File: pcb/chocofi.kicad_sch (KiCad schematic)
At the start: 154 parts, among them SW10 SW_PUSH, SW11 SW_PUSH, SW12 SW_PUSH, SW14 SW_PUSH, SW15 SW_PUSH, SW16 SW_PUSH, SW17 SW_PUSH, SW18 SW_PUSH, SW19 SW_PUSH, SW2 SW_PUSH, SW20 SW_PUSH, SW21 SW_PUSH, SW23 SW_PUSH, SW24 SW_PUSH, SW25 SW_PUSH, SW26 SW_PUSH, SW27 SW_PUSH, SW29 SW_PUSH, SW3 SW_PUSH, SW30 SW_PUSH, SW31 SW_PUSH, SW32 SW_PUSH, SW33 SW_PUSH, SW35 SW_PUSH, SW36 SW_PUSH, SW37 SW_PUSH, SW38 SW_PUSH, SW39 SW_PUSH, SW4 SW_PUSH, SW40 SW_PUSH, SW41 SW_PUSH, SW42 SW_PUSH, SW5 SW_PUSH, SW6 SW_PUSH, SW8 SW_PUSH, SW9 SW_PUSH, U1 nice_nano, U2 nice_nano

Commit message: feat: update
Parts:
- C1, C10, C11, C12, C13, C14, C15, C16, C17, C18, C19, C2, C20, C21, C22, C23, C24, C25, C26, C27, C28, C29, C3, C30, C31, C32, C33, C34, C35, C36, C4, C5, C6, C7, C8, C9: footprint (none) -> Capacitor_SMD:C_0805_2012Metric_Pad1.18x1.45mm_HandSolder
- D10, D11, D12, D14, D15, D16, D17, D18, D19, D2, D20, D21, D23, D24, D25, D26, D27, D29, D3, D30, D31, D32, D33, D35, D36, D37, D38, D39, D4, D40, D41, D42, D5, D6, D8, D9: footprint kbd:D3_TH -> Diode_SMD:D_SOD-323_HandSoldering
- RSW1, RSW2: footprint kbd:ResetSW_1side -> Button_Switch_SMD:SW_SPST_TS-1088-xR020
- SW10, SW11, SW12, SW14, SW15, SW16, SW17, SW18, SW19, SW2, SW20, SW23, SW24, SW25, SW26, SW27, SW29, SW3, SW30, SW31, SW32, SW33, SW35, SW36, SW37, SW38, SW39, SW4, SW40, SW41, SW5, SW6, SW8, SW9: footprint kbd:CherryMX_Choc_1u -> kbd:ChocV1_V2_Hotswap
- SW21, SW42: footprint kbd:CherryMX_Choc_1.5u -> kbd:ChocV1_V2_Hotswap
- U1, U2: footprint (none) -> Library:nice_nano
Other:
- moved on the sheet: C1, C10, C11, C12, C13, C14, C15, C16, C17, C18, C19, C2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

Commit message: feat: update
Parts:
- removed Cap100nf2: C, Capacitor_SMD:C_0805_2012Metric_Pad1.18x1.45mm_HandSolder, symbol Device:C
- removed RSW2: SW_PUSH, Button_Switch_SMD:SW_SPST_TS-1088-xR020, symbol corne-light-rescue:SW_PUSH-kbd
- removed battery2, switch2: Conn_01x02_Pin, Connector_JST:JST_SH_BM02B-SRSS-TB_1x02-1MP_P1.00mm_Vertical, symbol Connector:Conn_01x02_Pin
- added H1, H2, H3, H4, H5, H6, H7: MountingHole, MountingHole:MountingHole_2.2mm_M2_DIN965_Pad, symbol Mechanical:MountingHole
- C1, C10, C11, C12, C13, C14, C15, C16, C17, C18, C19, C2, C3, C4, C5, C6, C7, C8, C9: value 100nF -> Cap100nf
- C20: renamed from C21; value 100nF -> Cap100nf
- C21: renamed from C23; value 100nF -> Cap100nf
- C22: renamed from C25; value 100nF -> Cap100nf
- C23: renamed from C27; value 100nF -> Cap100nf
- C24: renamed from C29; value 100nF -> Cap100nf
- C25: renamed from C31; value 100nF -> Cap100nf
- C26: renamed from C33; value 100nF -> Cap100nf
- C27: renamed from C35; value 100nF -> Cap100nf
- C28: renamed from C36; value 100nF -> Cap100nf
- C29: renamed from C20; value 100nF -> Cap100nf
- C30: renamed from C22; value 100nF -> Cap100nf
- C31: renamed from C24; value 100nF -> Cap100nf
- C32: renamed from C26; value 100nF -> Cap100nf
- C33: renamed from C28; value 100nF -> Cap100nf
- C34: renamed from C30; value 100nF -> Cap100nf
- C35: renamed from C32; value 100nF -> Cap100nf
- C36: renamed from C34; value 100nF -> Cap100nf
- Cap100nf1: value C -> C_general
- LED1: renamed from D7; footprint LED_SMD:LED_SK6812MINI_PLCC4_3.5x3.5mm_P1.75mm -> kbd:YS-SK6812MINI-E
- LED10: renamed from D46; footprint LED_SMD:LED_SK6812MINI_PLCC4_3.5x3.5mm_P1.75mm -> kbd:YS-SK6812MINI-E
- LED11: renamed from D47; footprint LED_SMD:LED_SK6812MINI_PLCC4_3.5x3.5mm_P1.75mm -> kbd:YS-SK6812MINI-E
- LED12: renamed from D48; footprint LED_SMD:LED_SK6812MINI_PLCC4_3.5x3.5mm_P1.75mm -> kbd:YS-SK6812MINI-E
- LED13: renamed from D49; footprint LED_SMD:LED_SK6812MINI_PLCC4_3.5x3.5mm_P1.75mm -> kbd:YS-SK6812MINI-E
- LED14: renamed from D50; footprint LED_SMD:LED_SK6812MINI_PLCC4_3.5x3.5mm_P1.75mm -> kbd:YS-SK6812MINI-E
- LED15: renamed from D51; footprint LED_SMD:LED_SK6812MINI_PLCC4_3.5x3.5mm_P1.75mm -> kbd:YS-SK6812MINI-E
- LED16: renamed from D52; footprint LED_SMD:LED_SK6812MINI_PLCC4_3.5x3.5mm_P1.75mm -> kbd:YS-SK6812MINI-E
- LED17: renamed from D53; footprint LED_SMD:LED_SK6812MINI_PLCC4_3.5x3.5mm_P1.75mm -> kbd:YS-SK6812MINI-E
- LED18: renamed from D54; footprint LED_SMD:LED_SK6812MINI_PLCC4_3.5x3.5mm_P1.75mm -> kbd:YS-SK6812MINI-E
- LED19: renamed from D55; footprint LED_SMD:LED_SK6812MINI_PLCC4_3.5x3.5mm_P1.75mm -> kbd:YS-SK6812MINI-E
- LED2: renamed from D1; footprint LED_SMD:LED_SK6812MINI_PLCC4_3.5x3.5mm_P1.75mm -> kbd:YS-SK6812MINI-E
- LED20: renamed from D57; footprint LED_SMD:LED_SK6812MINI_PLCC4_3.5x3.5mm_P1.75mm -> kbd:YS-SK6812MINI-E
- LED21: renamed from D59; footprint LED_SMD:LED_SK6812MINI_PLCC4_3.5x3.5mm_P1.75mm -> kbd:YS-SK6812MINI-E
- LED22: renamed from D61; footprint LED_SMD:LED_SK6812MINI_PLCC4_3.5x3.5mm_P1.75mm -> kbd:YS-SK6812MINI-E
- LED23: renamed from D63; footprint LED_SMD:LED_SK6812MINI_PLCC4_3.5x3.5mm_P1.75mm -> kbd:YS-SK6812MINI-E
- LED24: renamed from D65; footprint LED_SMD:LED_SK6812MINI_PLCC4_3.5x3.5mm_P1.75mm -> kbd:YS-SK6812MINI-E
- LED25: renamed from D67; footprint LED_SMD:LED_SK6812MINI_PLCC4_3.5x3.5mm_P1.75mm -> kbd:YS-SK6812MINI-E
- LED26: renamed from D69; footprint LED_SMD:LED_SK6812MINI_PLCC4_3.5x3.5mm_P1.75mm -> kbd:YS-SK6812MINI-E
- LED27: renamed from D71; footprint LED_SMD:LED_SK6812MINI_PLCC4_3.5x3.5mm_P1.75mm -> kbd:YS-SK6812MINI-E
- LED28: renamed from D72; footprint LED_SMD:LED_SK6812MINI_PLCC4_3.5x3.5mm_P1.75mm -> kbd:YS-SK6812MINI-E
- LED29: renamed from D56; footprint LED_SMD:LED_SK6812MINI_PLCC4_3.5x3.5mm_P1.75mm -> kbd:YS-SK6812MINI-E
- LED3: renamed from D13; footprint LED_SMD:LED_SK6812MINI_PLCC4_3.5x3.5mm_P1.75mm -> kbd:YS-SK6812MINI-E
- LED30: renamed from D58; footprint LED_SMD:LED_SK6812MINI_PLCC4_3.5x3.5mm_P1.75mm -> kbd:YS-SK6812MINI-E
- LED31: renamed from D60; footprint LED_SMD:LED_SK6812MINI_PLCC4_3.5x3.5mm_P1.75mm -> kbd:YS-SK6812MINI-E
- LED32: renamed from D62; footprint LED_SMD:LED_SK6812MINI_PLCC4_3.5x3.5mm_P1.75mm -> kbd:YS-SK6812MINI-E
- LED33: renamed from D64; footprint LED_SMD:LED_SK6812MINI_PLCC4_3.5x3.5mm_P1.75mm -> kbd:YS-SK6812MINI-E
- LED34: renamed from D66; footprint LED_SMD:LED_SK6812MINI_PLCC4_3.5x3.5mm_P1.75mm -> kbd:YS-SK6812MINI-E
- LED35: renamed from D68; footprint LED_SMD:LED_SK6812MINI_PLCC4_3.5x3.5mm_P1.75mm -> kbd:YS-SK6812MINI-E
- LED36: renamed from D70; footprint LED_SMD:LED_SK6812MINI_PLCC4_3.5x3.5mm_P1.75mm -> kbd:YS-SK6812MINI-E
- LED4: renamed from D22; footprint LED_SMD:LED_SK6812MINI_PLCC4_3.5x3.5mm_P1.75mm -> kbd:YS-SK6812MINI-E
- LED5: renamed from D28; footprint LED_SMD:LED_SK6812MINI_PLCC4_3.5x3.5mm_P1.75mm -> kbd:YS-SK6812MINI-E
- LED6: renamed from D34; footprint LED_SMD:LED_SK6812MINI_PLCC4_3.5x3.5mm_P1.75mm -> kbd:YS-SK6812MINI-E
- LED7: renamed from D43; footprint LED_SMD:LED_SK6812MINI_PLCC4_3.5x3.5mm_P1.75mm -> kbd:YS-SK6812MINI-E
- LED8: renamed from D44; footprint LED_SMD:LED_SK6812MINI_PLCC4_3.5x3.5mm_P1.75mm -> kbd:YS-SK6812MINI-E
- LED9: renamed from D45; footprint LED_SMD:LED_SK6812MINI_PLCC4_3.5x3.5mm_P1.75mm -> kbd:YS-SK6812MINI-E
- SW1: renamed from SW2; footprint kbd:ChocV1_V2_Hotswap -> keyswitches:Kailh_socket_PG1350_reversible
- SW10: renamed from SW12; footprint kbd:ChocV1_V2_Hotswap -> keyswitches:Kailh_socket_PG1350_reversible
- SW11: renamed from SW14; footprint kbd:ChocV1_V2_Hotswap -> keyswitches:Kailh_socket_PG1350_reversible
- SW12: renamed from SW15; footprint kbd:ChocV1_V2_Hotswap -> keyswitches:Kailh_socket_PG1350_reversible
- SW13: renamed from SW16; footprint kbd:ChocV1_V2_Hotswap -> keyswitches:Kailh_socket_PG1350_reversible
- SW14: renamed from SW17; footprint kbd:ChocV1_V2_Hotswap -> keyswitches:Kailh_socket_PG1350_reversible
- SW15: renamed from SW18; footprint kbd:ChocV1_V2_Hotswap -> keyswitches:Kailh_socket_PG1350_reversible
- SW16: renamed from SW19; footprint kbd:ChocV1_V2_Hotswap -> keyswitches:Kailh_socket_PG1350_reversible
- SW17: renamed from SW20; footprint kbd:ChocV1_V2_Hotswap -> keyswitches:Kailh_socket_PG1350_reversible
- SW18: renamed from SW21; footprint kbd:ChocV1_V2_Hotswap -> keyswitches:Kailh_socket_PG1350_reversible
- SW19: renamed from SW23; footprint kbd:ChocV1_V2_Hotswap -> keyswitches:Kailh_socket_PG1350_reversible
- SW2: renamed from SW3; footprint kbd:ChocV1_V2_Hotswap -> keyswitches:Kailh_socket_PG1350_reversible
- SW20: renamed from SW24; footprint kbd:ChocV1_V2_Hotswap -> keyswitches:Kailh_socket_PG1350_reversible
- SW21: renamed from SW25; footprint kbd:ChocV1_V2_Hotswap -> keyswitches:Kailh_socket_PG1350_reversible
- SW22: renamed from SW26; footprint kbd:ChocV1_V2_Hotswap -> keyswitches:Kailh_socket_PG1350_reversible
- SW23: renamed from SW27; footprint kbd:ChocV1_V2_Hotswap -> keyswitches:Kailh_socket_PG1350_reversible
- SW24: renamed from SW29; footprint kbd:ChocV1_V2_Hotswap -> keyswitches:Kailh_socket_PG1350_reversible
- SW25: renamed from SW30; footprint kbd:ChocV1_V2_Hotswap -> keyswitches:Kailh_socket_PG1350_reversible
- SW26: renamed from SW31; footprint kbd:ChocV1_V2_Hotswap -> keyswitches:Kailh_socket_PG1350_reversible
- SW27: renamed from SW32; footprint kbd:ChocV1_V2_Hotswap -> keyswitches:Kailh_socket_PG1350_reversible
- SW28: renamed from SW33; footprint kbd:ChocV1_V2_Hotswap -> keyswitches:Kailh_socket_PG1350_reversible
- SW29: renamed from SW35; footprint kbd:ChocV1_V2_Hotswap -> keyswitches:Kailh_socket_PG1350_reversible
- SW3: renamed from SW4; footprint kbd:ChocV1_V2_Hotswap -> keyswitches:Kailh_socket_PG1350_reversible
- SW30: renamed from SW36; footprint kbd:ChocV1_V2_Hotswap -> keyswitches:Kailh_socket_PG1350_reversible
- SW31: renamed from SW37; footprint kbd:ChocV1_V2_Hotswap -> keyswitches:Kailh_socket_PG1350_reversible
- SW32: renamed from SW38; footprint kbd:ChocV1_V2_Hotswap -> keyswitches:Kailh_socket_PG1350_reversible
- SW33: renamed from SW39; footprint kbd:ChocV1_V2_Hotswap -> keyswitches:Kailh_socket_PG1350_reversible
- SW34: renamed from SW40; footprint kbd:ChocV1_V2_Hotswap -> keyswitches:Kailh_socket_PG1350_reversible
- SW35: renamed from SW41; footprint kbd:ChocV1_V2_Hotswap -> keyswitches:Kailh_socket_PG1350_reversible
- SW36: renamed from SW42; footprint kbd:ChocV1_V2_Hotswap -> keyswitches:Kailh_socket_PG1350_reversible
- SW4: renamed from SW5; footprint kbd:ChocV1_V2_Hotswap -> keyswitches:Kailh_socket_PG1350_reversible
- SW5: renamed from SW6; footprint kbd:ChocV1_V2_Hotswap -> keyswitches:Kailh_socket_PG1350_reversible
- SW6: renamed from SW8; footprint kbd:ChocV1_V2_Hotswap -> keyswitches:Kailh_socket_PG1350_reversible
- SW7: renamed from SW9; footprint kbd:ChocV1_V2_Hotswap -> keyswitches:Kailh_socket_PG1350_reversible
- SW8: renamed from SW10; footprint kbd:ChocV1_V2_Hotswap -> keyswitches:Kailh_socket_PG1350_reversible
- SW9: renamed from SW11; footprint kbd:ChocV1_V2_Hotswap -> keyswitches:Kailh_socket_PG1350_reversible
- renumbered D2 to D1, D12 to D10, D14 to D11, D15 to D12, D16 to D13, D17 to D14, D18 to D15, D19 to D16, D20 to D17, D21 to D18, D23 to D19, D3 to D2, D24 to D20, D25 to D21, D26 to D22, D27 to D23, D29 to D24, D30 to D25, D31 to D26, D32 to D27, D33 to D28, D35 to D29, D4 to D3, D36 to D30, D37 to D31, D38 to D32, D39 to D33, D40 to D34, D41 to D35, D42 to D36, D5 to D4, D6 to D5, D8 to D6, D9 to D7, D10 to D8, D11 to D9
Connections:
- net BAT_r is gone; now on net BAT: U2.24 (BATIN/P0.04)
- net LED_r is gone; now on net LED: LED19.3 (DIN), U2.2 (RX1/P0.08)
- net VDD is gone; now on net VCC: C19.2, C20.2, C21.2, C22.2, C23.2, C24.2, C25.2, C26.2, C27.2, C28.2, C29.2, C30.2, C31.2, C32.2, C33.2, C34.2, C35.2, C36.2, U2.21 (VCC)
- net col5_r is gone; now on net col4_r: SW23.1, SW28.1, SW33.1, SW36.1
- net nice!view_CSL_r is gone; now on net nice!view_CSL: U2.6 (P0.20)
- net nice!view_CS_r is gone; now on net nice!view_CS: U2.1 (TX0/P0.06)
- net nice!view_MOSI_r is gone; now on net nice!view_MOSI: U2.5 (P0.17)
- net reset_r is gone; now on net reset: U2.22 (RST)
- net GND: now also LED19.4 (VDD), LED20.4 (VDD), LED21.4 (VDD), LED22.4 (VDD), LED23.4 (VDD), LED24.4 (VDD), LED25.4 (VDD), LED26.4 (VDD), LED27.4 (VDD), LED28.4 (VDD), LED29.4 (VDD), LED30.4 (VDD), LED31.4 (VDD), LED32.4 (VDD), LED33.4 (VDD), LED34.4 (VDD), LED35.4 (VDD), LED36.4 (VDD), U2.23 (GND)
- net GNDA: no longer LED19.4 (VDD), LED20.4 (VDD), LED21.4 (VDD), LED22.4 (VDD), LED23.4 (VDD), LED24.4 (VDD), LED25.4 (VDD), LED26.4 (VDD), LED27.4 (VDD), LED28.4 (VDD), LED29.4 (VDD), LED30.4 (VDD), LED31.4 (VDD), LED32.4 (VDD), LED33.4 (VDD), LED34.4 (VDD), LED35.4 (VDD), LED36.4 (VDD), U2.23 (GND)
- net LED: now also LED5.1 (DOUT); no longer LED1.3 (DIN)
- net col0_r: now also SW19.1, SW24.1, SW29.1
- net col1_r: now also SW20.1, SW25.1, SW30.1; no longer SW19.1, SW24.1, SW29.1
- net col2_r: now also SW21.1, SW26.1, SW31.1, SW34.1; no longer SW20.1, SW25.1, SW30.1
- net col3_r: now also SW22.1, SW27.1, SW32.1, SW35.1; no longer SW21.1, SW26.1, SW31.1, SW34.1
- net col4_r: no longer SW22.1, SW27.1, SW32.1, SW35.1
- net at LED33.1 (DOUT): now also LED36.1 (DOUT); no longer LED34.3 (DIN)
- net at LED16.3 (DIN): now also LED11.3 (DIN); no longer LED15.1 (DOUT)
- net at LED23.1 (DOUT): now also LED28.1 (DOUT); no longer LED24.3 (DIN)
- net at LED6.3 (DIN): now also LED1.3 (DIN); no longer LED5.1 (DOUT)
- net LED_bis: no longer names the net of LED10.1 (DOUT)
- net LED_bis: now also LED15.1 (DOUT); no longer LED11.3 (DIN)
- net LED_bis_r: no longer names the net of LED29.3 (DIN)
- net LED_bis_r: now also LED24.3 (DIN); no longer LED28.1 (DOUT)
- no-connect marks 16 -> 10
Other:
- moved on the sheet: C1, C10, C11, C12, C13, C14, C15, C16, C17, C18, C19, C2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

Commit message: feat(pcb/schematic): update footprint for switch + nice!view socket
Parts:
- removed C19, C20, C21, C22, C23, C24, C25, C26, C27, C28, C29, C30, C31, C32, C33, C34, C35, C36: Cap100nf, Capacitor_SMD:C_0805_2012Metric_Pad1.18x1.45mm_HandSolder, symbol Device:C
- removed D19, D20, D21, D22, D23, D24, D25, D26, D27, D28, D29, D30, D31, D32, D33, D34, D35, D36: D, Diode_SMD:D_SOD-323_HandSoldering, symbol Device:D
- removed LED19, LED20, LED21, LED22, LED23, LED24, LED25, LED26, LED27, LED28, LED29, LED30, LED31, LED32, LED33, LED34, LED35, LED36: SK6812MINI, kbd:YS-SK6812MINI-E, symbol LED:SK6812MINI
- removed SW19, SW20, SW21, SW22, SW23, SW24, SW25, SW26, SW27, SW28, SW29, SW30, SW31, SW32, SW33, SW34, SW35, SW36: SW_PUSH, keyswitches:Kailh_socket_PG1350_reversible, symbol corne-light-rescue:SW_PUSH-kbd
- removed U2: nice_nano, Library:nice_nano, symbol nice_nano:nice_nano
- added nice!view: Conn_01x05_MountingPin, symbol Connector_Generic_MountingPin:Conn_01x05_MountingPin
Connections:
- net GND: now also nice!view.4 (Pin_4)
- net VCC: now also nice!view.3 (Pin_3)
- net nice!view_CS: now also nice!view.5 (Pin_5)
- net nice!view_CSL: now also nice!view.2 (Pin_2)
- net nice!view_MOSI: now also nice!view.1 (Pin_1)
- no-connect marks 10 -> 5
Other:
- moved on the sheet: C1, C10, C11, C12, C13, C14, C15, C16, C17, C18, C2, C3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

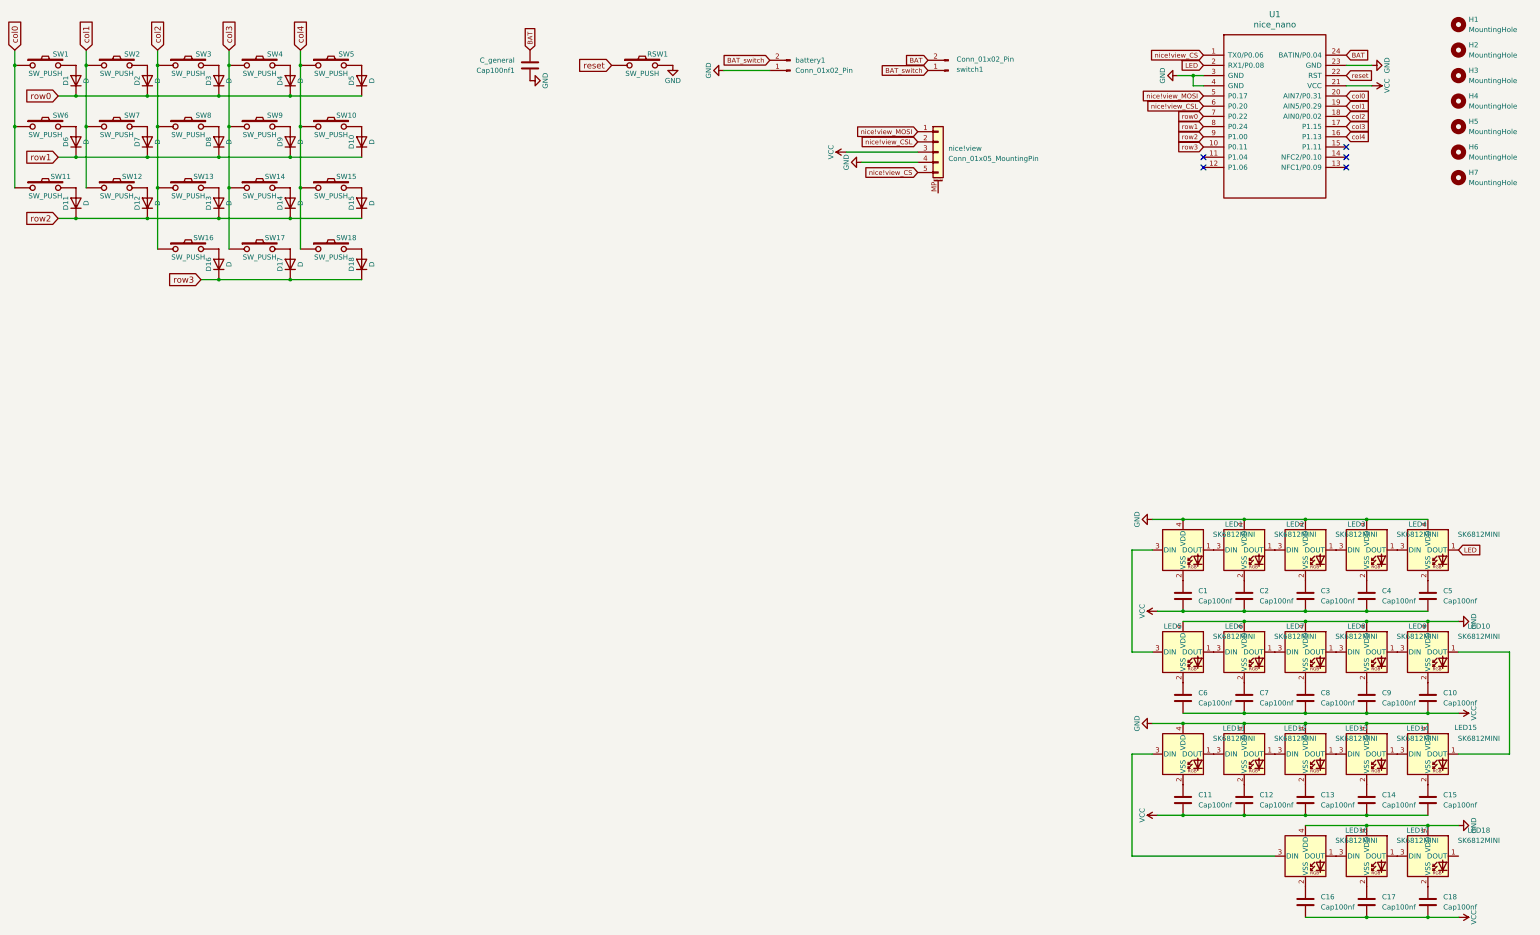
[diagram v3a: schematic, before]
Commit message: feat(pcb/schematic): update LED handling
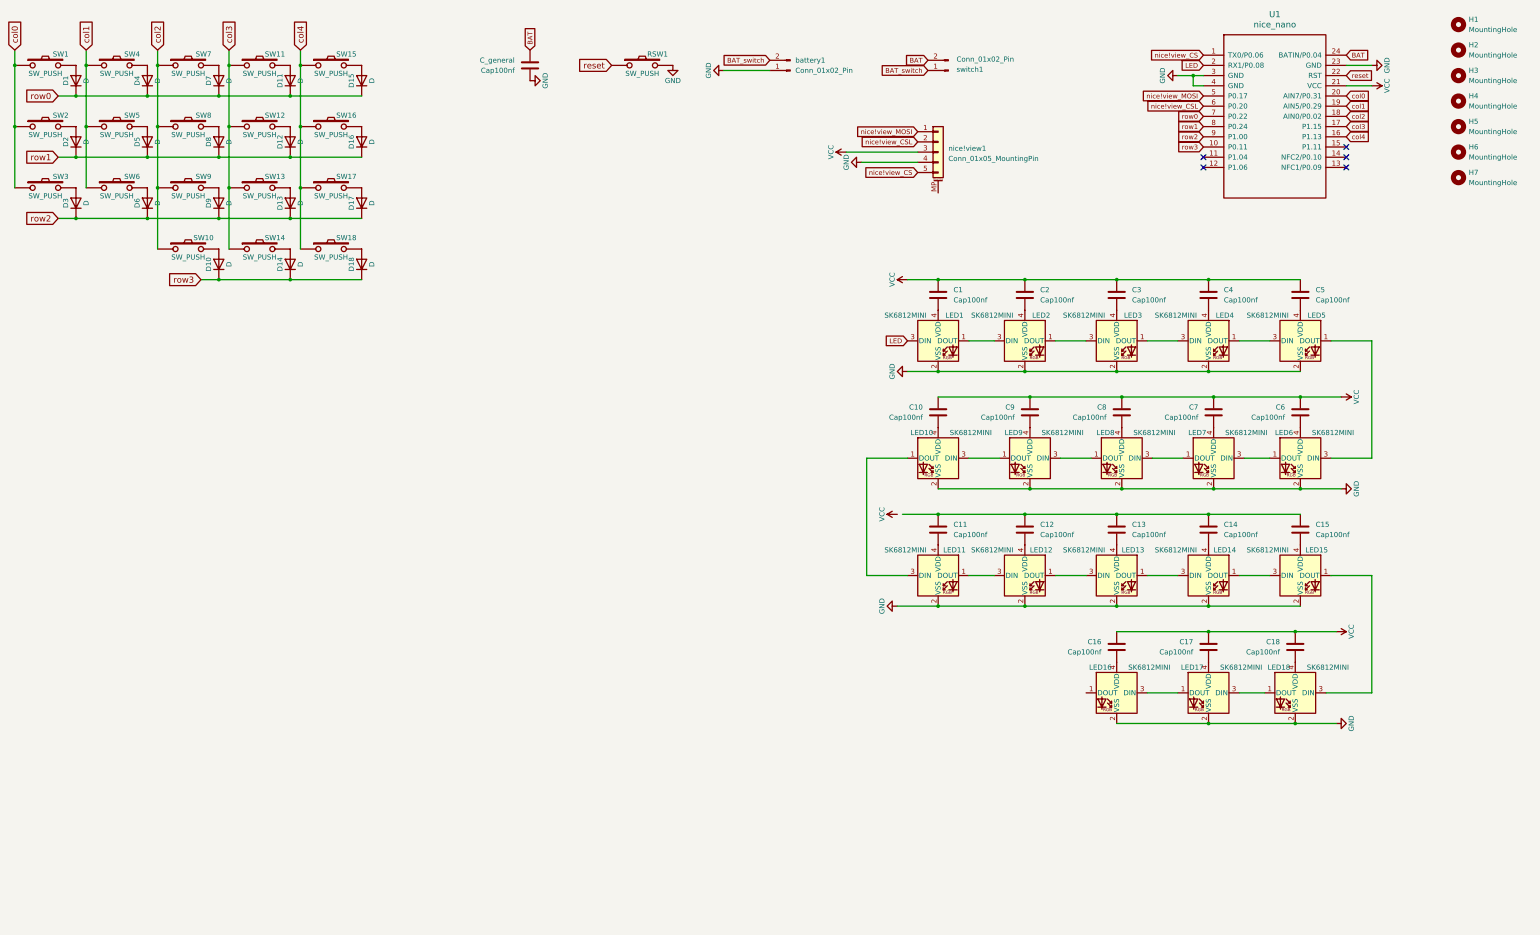
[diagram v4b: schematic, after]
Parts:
- SW1, SW18, SW8: footprint keyswitches:Kailh_socket_PG1350_reversible -> PCM_Switch_Keyboard_Hotswap_Kailh:SW_Hotswap_Kailh_Choc_V1V2_Plated
- SW10: renamed from SW16; footprint keyswitches:Kailh_socket_PG1350_reversible -> PCM_Switch_Keyboard_Hotswap_Kailh:SW_Hotswap_Kailh_Choc_V1V2_Plated
- SW11: renamed from SW4; footprint keyswitches:Kailh_socket_PG1350_reversible -> PCM_Switch_Keyboard_Hotswap_Kailh:SW_Hotswap_Kailh_Choc_V1V2_Plated
- SW12: renamed from SW9; footprint keyswitches:Kailh_socket_PG1350_reversible -> PCM_Switch_Keyboard_Hotswap_Kailh:SW_Hotswap_Kailh_Choc_V1V2_Plated
- SW13: renamed from SW14; footprint keyswitches:Kailh_socket_PG1350_reversible -> PCM_Switch_Keyboard_Hotswap_Kailh:SW_Hotswap_Kailh_Choc_V1V2_Plated
- SW14: renamed from SW17; footprint keyswitches:Kailh_socket_PG1350_reversible -> PCM_Switch_Keyboard_Hotswap_Kailh:SW_Hotswap_Kailh_Choc_V1V2_Plated
- SW15: renamed from SW5; footprint keyswitches:Kailh_socket_PG1350_reversible -> PCM_Switch_Keyboard_Hotswap_Kailh:SW_Hotswap_Kailh_Choc_V1V2_Plated
- SW16: renamed from SW10; footprint keyswitches:Kailh_socket_PG1350_reversible -> PCM_Switch_Keyboard_Hotswap_Kailh:SW_Hotswap_Kailh_Choc_V1V2_Plated
- SW17: renamed from SW15; footprint keyswitches:Kailh_socket_PG1350_reversible -> PCM_Switch_Keyboard_Hotswap_Kailh:SW_Hotswap_Kailh_Choc_V1V2_Plated
- SW2: renamed from SW6; footprint keyswitches:Kailh_socket_PG1350_reversible -> PCM_Switch_Keyboard_Hotswap_Kailh:SW_Hotswap_Kailh_Choc_V1V2_Plated
- SW3: renamed from SW11; footprint keyswitches:Kailh_socket_PG1350_reversible -> PCM_Switch_Keyboard_Hotswap_Kailh:SW_Hotswap_Kailh_Choc_V1V2_Plated
- SW4: renamed from SW2; footprint keyswitches:Kailh_socket_PG1350_reversible -> PCM_Switch_Keyboard_Hotswap_Kailh:SW_Hotswap_Kailh_Choc_V1V2_Plated
- SW5: renamed from SW7; footprint keyswitches:Kailh_socket_PG1350_reversible -> PCM_Switch_Keyboard_Hotswap_Kailh:SW_Hotswap_Kailh_Choc_V1V2_Plated
- SW6: renamed from SW12; footprint keyswitches:Kailh_socket_PG1350_reversible -> PCM_Switch_Keyboard_Hotswap_Kailh:SW_Hotswap_Kailh_Choc_V1V2_Plated
- SW7: renamed from SW3; footprint keyswitches:Kailh_socket_PG1350_reversible -> PCM_Switch_Keyboard_Hotswap_Kailh:SW_Hotswap_Kailh_Choc_V1V2_Plated
- SW9: renamed from SW13; footprint keyswitches:Kailh_socket_PG1350_reversible -> PCM_Switch_Keyboard_Hotswap_Kailh:SW_Hotswap_Kailh_Choc_V1V2_Plated
- nice!view1: renamed from nice!view; footprint (none) -> Connector_PinHeader_2.54mm:PinHeader_1x05_P2.54mm_Vertical
- renumbered Cap100nf1 to Cap100nf, D16 to D10, D4 to D11, D9 to D12, D14 to D13, D17 to D14, D5 to D15, D10 to D16, D15 to D17, D6 to D2, D11 to D3, D2 to D4, D7 to D5, D12 to D6, D3 to D7, D13 to D9
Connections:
- net GND: now also LED1.2 (VSS), LED10.2 (VSS), LED11.2 (VSS), LED12.2 (VSS), LED13.2 (VSS), LED14.2 (VSS), LED15.2 (VSS), LED16.2 (VSS), LED17.2 (VSS), LED18.2 (VSS), LED2.2 (VSS), LED3.2 (VSS), LED4.2 (VSS), LED5.2 (VSS), LED6.2 (VSS), LED7.2 (VSS), LED8.2 (VSS), LED9.2 (VSS); no longer LED1.4 (VDD), LED10.4 (VDD), LED11.4 (VDD), LED12.4 (VDD), LED13.4 (VDD), LED14.4 (VDD), LED15.4 (VDD), LED16.4 (VDD), LED17.4 (VDD), LED18.4 (VDD), LED2.4 (VDD), LED3.4 (VDD), LED4.4 (VDD), LED5.4 (VDD), LED6.4 (VDD), LED7.4 (VDD), LED8.4 (VDD), LED9.4 (VDD)
- net LED: now also LED1.3 (DIN); no longer LED5.1 (DOUT)
- net VCC: now also C1.1, C10.1, C16.1, C17.1, C18.1, C2.1, C3.1, C4.1, C5.1, C6.1, C7.1, C8.1, C9.1; no longer C1.2, C10.2, C11.2, C12.2, C13.2, C14.2, C15.2, C16.2, C17.2, C18.2, C2.2, C3.2, C4.2, C5.2, C6.2, C7.2, C8.2, C9.2
- net at C11.1: now also C12.1, C13.1, C14.1, C15.1; no longer LED11.2 (VSS)
- net at LED16.1 (DOUT): no longer LED17.3 (DIN)
- net at LED16.3 (DIN): now also LED17.1 (DOUT); no longer LED11.3 (DIN)
- net at LED15.1 (DOUT): now also LED18.3 (DIN); no longer LED10.1 (DOUT)
- net at LED6.3 (DIN): now also LED5.1 (DOUT); no longer LED1.3 (DIN)
- net at LED18.1 (DOUT): now also LED17.3 (DIN)
- new net: C1.2, LED1.4 (VDD)
- new net: C2.2, LED2.4 (VDD)
- new net: C9.2, LED9.4 (VDD)
- new net: C16.2, LED16.4 (VDD)
- new net: C12.2, LED12.4 (VDD)
- new net: C13.2, LED13.4 (VDD)
- new net: C5.2, LED5.4 (VDD)
- new net: C18.2, LED18.4 (VDD)
- new net: C4.2, LED4.4 (VDD)
- new net: LED10.1 (DOUT), LED11.3 (DIN)
- new net: C10.2, LED10.4 (VDD)
- new net: C11.2, LED11.4 (VDD)
- new net: C6.2, LED6.4 (VDD)
- new net: C3.2, LED3.4 (VDD)
- new net: C15.2, LED15.4 (VDD)
- new net: C14.2, LED14.4 (VDD)
- new net: C17.2, LED17.4 (VDD)
- new net: C8.2, LED8.4 (VDD)
- new net: C7.2, LED7.4 (VDD)

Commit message: feat(pcb): upgrade
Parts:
- C1, C10, C11, C12, C13, C14, C15, C16, C17, C18, C2, C3, C4, C5, C6, C7, C8, C9: footprint Capacitor_SMD:C_0805_2012Metric_Pad1.18x1.45mm_HandSolder -> Library:C_0805_2012Metric_Pad1.18x1.45mm_HandSolder_Custom
- C_BAT: renamed from Cap100nf; value C_general -> Cap100nf
- D1, D10, D11, D12, D13, D14, D15, D16, D17, D18, D2, D3, D4, D5, D6, D7, D8, D9: footprint Diode_SMD:D_SOD-323_HandSoldering -> Library:D_SOD-323_HandSoldering_Custom
- renumbered LED18 to LED16, LED16 to LED18
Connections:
- net VCC: now also C11.1, C12.1, C13.1, C14.1, C15.1
- net at LED18.4 (VDD): now also C18.2; no longer C16.2
- net at LED16.4 (VDD): now also C16.2; no longer C18.2

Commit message: feat(pcb): update it
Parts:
- battery1, switch1: footprint Connector_JST:JST_SH_BM02B-SRSS-TB_1x02-1MP_P1.00mm_Vertical -> Library:JST_SH_SM02B-SRSS-TB_1x02-1MP_P1.00mm_Horizontal_Custom
- renumbered C_BAT to C_BAT1
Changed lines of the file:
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@@
 			)
 		)
-		(property "Footprint" "Connector_JST:JST_SH_BM02B-SRSS-TB_1x02-1MP_P1.00mm_Vertical"
+		(property "Footprint" "Library:JST_SH_SM02B-SRSS-TB_1x02-1MP_P1.00mm_Horizontal_Custom"
 			(at 218.44 31.75 0)
 			(effects
@@
 			)
 		)
-		(property "Footprint" "Connector_JST:JST_SH_BM02B-SRSS-TB_1x02-1MP_P1.00mm_Vertical"
+		(property "Footprint" "Library:JST_SH_SM02B-SRSS-TB_1x02-1MP_P1.00mm_Horizontal_Custom"
 			(at 257.81 31.75 0)
 			(effects
@@
 		(on_board yes)
 		(dnp no)
-		(property "Reference" "C_BAT"
+		(property "Reference" "C_BAT1"
 			(at 149.86 31.7501 0)
 			(effects
@@
 			(project "chocofi"
 				(path "/2e32ab7e-c9fb-4e05-9497-0d2aa8a6c3fa"
-					(reference "C_BAT")
-					(unit 1)
-				)
+					(reference "C_BAT1")
+					(unit 1)
+				)

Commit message: feat(pcb): have a good version
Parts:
- C1, C10, C11, C12, C13, C14, C15, C16, C17, C18, C2, C3, C4, C5, C6, C7, C8, C9: footprint Library:C_0805_2012Metric_Pad1.18x1.45mm_HandSolder_Custom -> chocofi:C_0805_2012Metric_Pad1.18x1.45mm_HandSolder
- C_BAT1: footprint Capacitor_SMD:C_0805_2012Metric_Pad1.18x1.45mm_HandSolder -> chocofi:C_0805_2012Metric_Pad1.18x1.45mm_HandSolder
- D1, D10, D11, D12, D13, D14, D15, D16, D17, D18, D2, D3, D4, D5, D6, D7, D8, D9: footprint Library:D_SOD-323_HandSoldering_Custom -> chocofi:D_SOD-323_HandSoldering
- LED1, LED10, LED11, LED12, LED13, LED14, LED15, LED16, LED17, LED18, LED2, LED3, LED4, LED5, LED6, LED7, LED8, LED9: footprint kbd:YS-SK6812MINI-E -> chocofi:YS-SK6812MINI-E
- SW1, SW10, SW11, SW12, SW13, SW14, SW15, SW16, SW17, SW18, SW2, SW3, SW4, SW5, SW6, SW7, SW8, SW9: footprint PCM_Switch_Keyboard_Hotswap_Kailh:SW_Hotswap_Kailh_Choc_V1V2_Plated -> chocofi:SW_Hotswap_Kailh_Choc_V1V2_Plated
- U1: footprint Library:nice_nano -> chocofi:nice_nano
- battery1, switch1: footprint Library:JST_SH_SM02B-SRSS-TB_1x02-1MP_P1.00mm_Horizontal_Custom -> chocofi:JST_SH_SM02B-SRSS-TB_1x02-1MP_P1.00mm_Horizontal
- nice!view1: footprint Connector_PinHeader_2.54mm:PinHeader_1x05_P2.54mm_Vertical -> chocofi:PinHeader_1x05_P2.54mm_Vertical
